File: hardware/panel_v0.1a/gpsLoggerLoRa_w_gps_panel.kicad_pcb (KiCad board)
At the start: 4 copper layers, 70.2 x 72.7 mm, 155 parts, among them J1 JST DF12 10P, J1 USB_C_Receptacle, J2 JST GH, J3 DF12 - 10P, J4 CTX TAG Connect, Q1 FG6943010R, SW1 SW_Push, U1 NEO_M8, U1 SKY13373, U2 BGU7007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

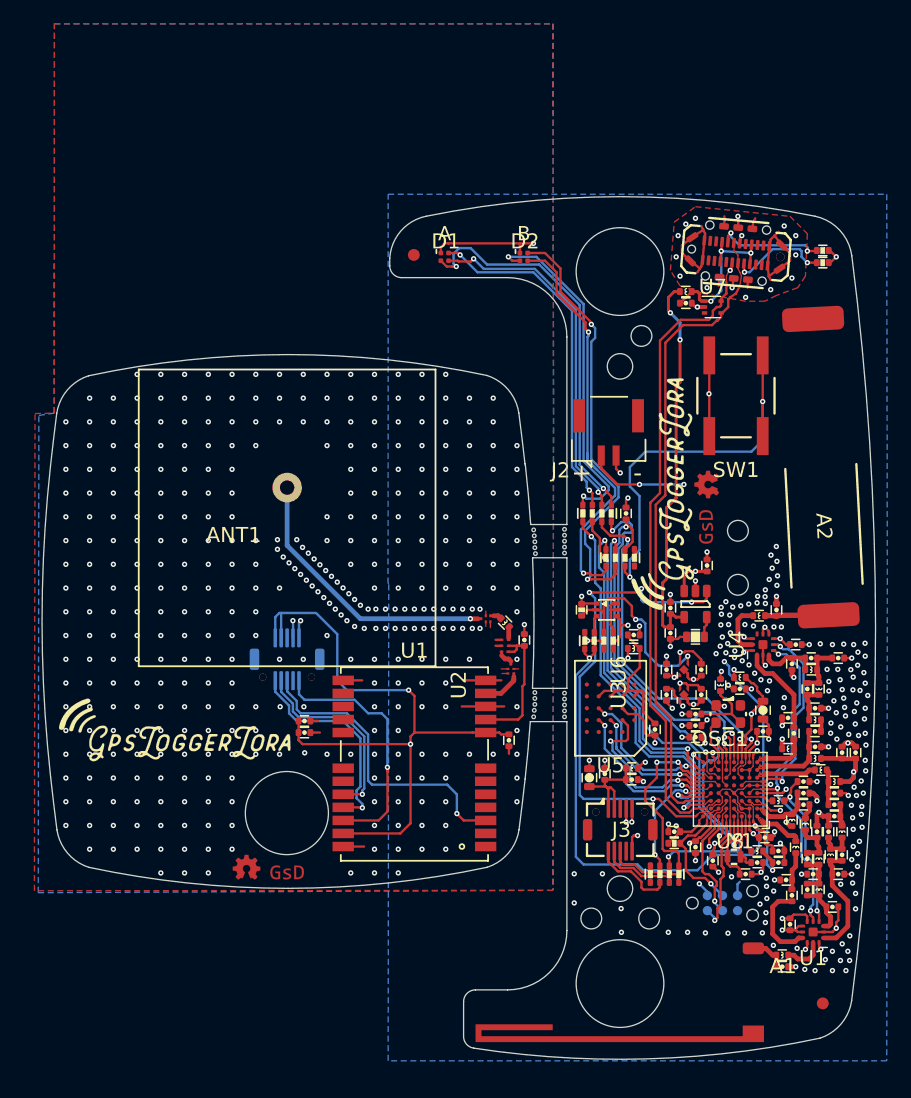
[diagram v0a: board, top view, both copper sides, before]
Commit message: Re-do panel with new changes from GPS PCB.
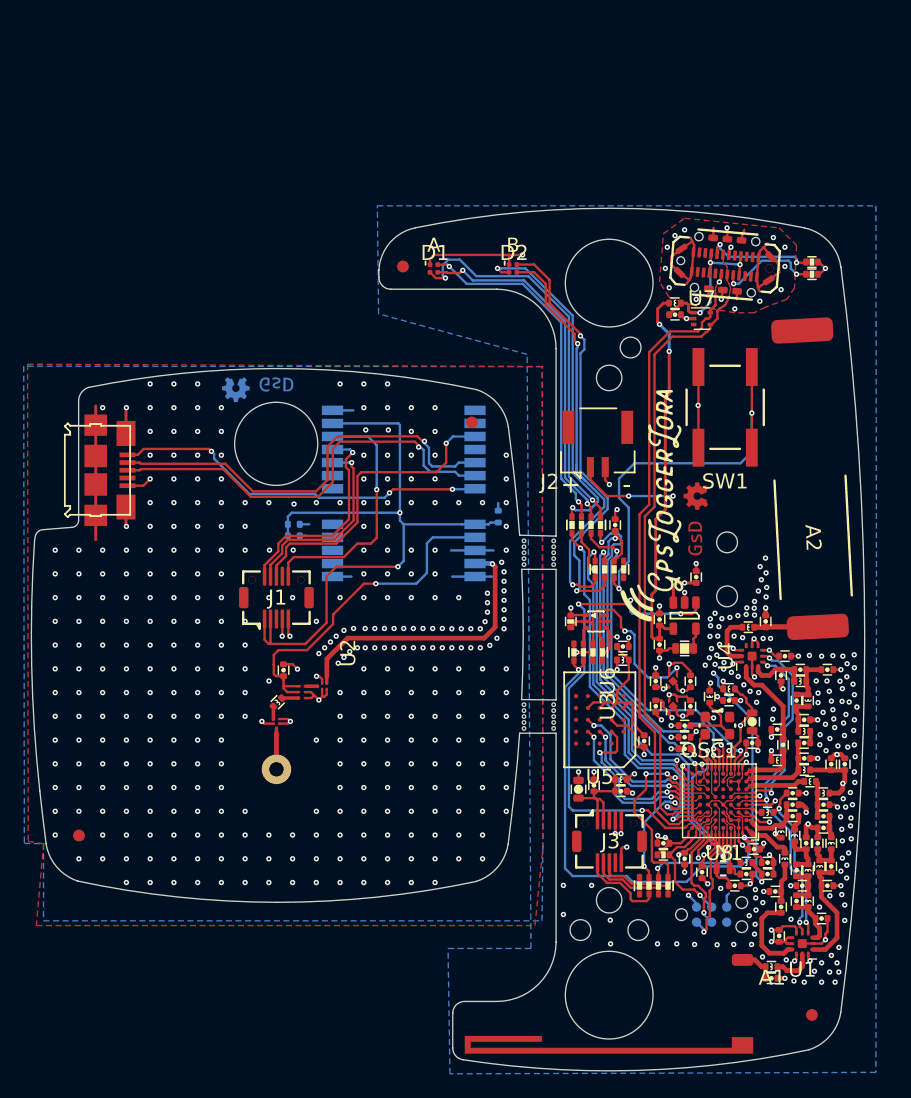
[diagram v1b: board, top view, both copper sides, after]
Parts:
- removed the G*** at (158.8, 94.0)
- removed the G*** at (158.8, 90.5)
- removed the G*** at (123.4, 123.2)
- removed the G*** at (120.0, 122.7)
- removed the REF** at (144.3, 108.0)
- removed the REF** at (144.2, 110.0)
- removed the REF** at (144.2, 94.3)
- removed the REF** at (144.3, 94.8)
- removed the REF** at (144.3, 95.8)
- removed the REF** at (144.3, 95.3)
- removed the REF** at (144.4, 96.3)
- removed the REF** at (144.3, 108.5)
- removed the REF** at (144.3, 109.0)
- removed the REF** at (144.3, 109.5)
- added G***: LOGO, gkl_logos:gsd_logo_small, F.Cu at (157.9, 95.0)
- added G***: LOGO, gkl_logos:oshw_small, F.Cu at (157.9, 91.4)
- added G***: LOGO, gkl_logos:gsd_logo_small, B.Cu at (122.5, 81.9)
- added G***: LOGO, gkl_logos:oshw_small, B.Cu at (119.1, 82.4)
- added J2: USB_OTG, Connector_USB_Micro_B_SMD, F.Cu at (107.3, 89.3)
- added REF**: Fiducial_1mm_Dia_2.54mm_Outer_CopperBottom, Fiducials:Fiducial_1mm_Dia_2.54mm_Outer_CopperBottom, B.Cu at (105.9, 120.0)
- added REF**: M1.6_Mounting Hole, M1.6_Mounting Hole, B.Cu at (143.4, 110.5)
- added REF**: M1.6_Mounting Hole, M1.6_Mounting Hole, B.Cu at (143.4, 110.0)
- added REF**: M1.6_Mounting Hole, M1.6_Mounting Hole, B.Cu at (143.4, 109.0)
- added REF**: Fiducial_1mm_Dia_2.54mm_Outer_CopperBottom, Fiducials:Fiducial_1mm_Dia_2.54mm_Outer_CopperBottom, B.Cu at (139.0, 85.2)
- added REF**: M1.6_Mounting Hole, M1.6_Mounting Hole, F.Cu at (143.4, 95.2)
- added REF**: M1.6_Mounting Hole, M1.6_Mounting Hole, F.Cu at (143.4, 96.2)
- added REF**: M1.6_Mounting Hole, M1.6_Mounting Hole, F.Cu at (143.4, 96.7)
- added REF**: M1.6_Mounting Hole, M1.6_Mounting Hole, F.Cu at (143.4, 95.7)
- added REF**: M1.6_Mounting Hole, M1.6_Mounting Hole, F.Cu at (143.4, 97.2)
- added REF**: M1.6_Mounting Hole, M1.6_Mounting Hole, B.Cu at (143.4, 111.0)
- added REF**: M1.6_Mounting Hole, M1.6_Mounting Hole, B.Cu at (143.4, 109.5)
- ANT1, C1, C2, C3, G***, U1: moved to B.Cu
- J1: moved to F.Cu
- moved ANT1 23.7 mm to (122.5, 114.4)
- moved U1 22.8 mm to (133.3, 91.2)
- moved C4 20.4 mm to (123.1, 106.1)
- moved L1 20.3 mm to (122.6, 108.8), turned to 225 degrees
- moved FLT2 19.7 mm to (122.5, 110.6), turned to 90 degrees
- moved C3 18.9 mm to (141.2, 93.2), turned to 90 degrees
- moved C2 17.6 mm to (124.0, 93.8)
- moved U2 17.6 mm to (124.7, 107.9), turned to 270 degrees
- moved FLT1 16.0 mm to (126.4, 107.4), turned to 0 degrees
- moved C1 15.6 mm to (124.0, 94.8)
- moved G*** 13.1 mm to (113.1, 98.1), turned to 90 degrees
- moved J1 5.27 mm to (122.5, 100.0)
- moved L14 1.34 mm to (167.3, 123.0)
- moved L8 1.34 mm to (167.3, 108.7)
- moved R7 1.34 mm to (155.1, 121.7)
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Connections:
- U1 pad 5: Net-(U1-Pad5) -> /DATA_N
- U1 pad 6: Net-(U1-Pad6) -> /DATA_P
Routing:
- net /DATA_N: track 0.00 -> 35.9 mm, vias 0 -> 1
- net /DATA_P: track 0.00 -> 35.9 mm, vias 0 -> 1
- net Net-(J2-Pad1): track 0.00 -> 31.7 mm, vias 0 -> 3
- net GND: track 141.7 -> 164.0 mm, vias 591 -> 568
- net Net-(FLT1-Pad3): track 3.42 -> 24.2 mm, vias 0 -> 1
- net Net-(ANT1-Pad1): track 23.8 -> 3.47 mm, vias 1 -> 0
- net Net-(C4-Pad1): track 11.6 -> 29.2 mm, vias 0 -> 1
- net Net-(FLT1-Pad1): track 1.57 -> 1.02 mm
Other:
- outline, holes or cut-outs redrawn
